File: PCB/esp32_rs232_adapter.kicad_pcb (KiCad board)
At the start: 2 copper layers, 46.5 x 57.7 mm, 46 parts, among them J1 Conn_01x04_Male, J2 DB9, J4 USB_B_Micro, Q1 IRF7404, SW2 Null_Modem_Selector, SW3 SW_SPST, U1 ESP32-WROOM-32D, U2 MAX3232, U3 TP4056, U4 AMS1117

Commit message: remove via in through hole
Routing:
- net Net-(J2-Pad3): vias 1 -> 0
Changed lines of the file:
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@@
     (thickness 1.6)
     (drawings 11)
-    (tracks 338)
+    (tracks 337)
     (zones 0)
     (modules 46)
@@
   (segment (start 161.671 123.885) (end 156.144001 129.411999) (width 0.25) (layer F.Cu) (net 32))
   (segment (start 153.38037 129.794) (end 152.249 129.794) (width 0.25) (layer F.Cu) (net 32))
-  (via (at 155.019 129.794) (size 0.8) (drill 0.4) (layers F.Cu B.Cu) (net 33))
   (segment (start 156.591 122.415) (end 156.591 128.222) (width 0.25) (layer F.Cu) (net 33))
   (segment (start 156.591 128.222) (end 155.019 129.794) (width 0.25) (layer F.Cu) (net 33))

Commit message: update
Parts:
- U2: footprint Package_SO:SSOP-16_5.3x6.2mm_P0.65mm -> Package_SO:SOP-16_4.55x10.3mm_P1.27mm
- moved U2 1.92 mm to (153.9, 115.8)
- renumbered Flash to SW1
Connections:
- J2 pad 9: (no net) -> Net-(J2-Pad9)
- J4 pad 2: (no net) -> Net-(J4-Pad2)
- J4 pad 3: (no net) -> Net-(J4-Pad3)
- J4 pad 4: (no net) -> Net-(J4-Pad4)
- U1 pad 11: (no net) -> Net-(U1-Pad11)
- U1 pad 12: (no net) -> Net-(U1-Pad12)
- U1 pad 13: (no net) -> Net-(U1-Pad13)
- U1 pad 14: (no net) -> Net-(U1-Pad14)
- U1 pad 16: (no net) -> Net-(U1-Pad16)
- U1 pad 17: (no net) -> Net-(U1-Pad17)
- U1 pad 18: (no net) -> Net-(U1-Pad18)
- U1 pad 19: (no net) -> Net-(U1-Pad19)
- U1 pad 20: (no net) -> Net-(U1-Pad20)
- U1 pad 21: (no net) -> Net-(U1-Pad21)
- U1 pad 22: (no net) -> Net-(U1-Pad22)
- U1 pad 23: (no net) -> Net-(U1-Pad23)
- U1 pad 26: (no net) -> Net-(U1-Pad26)
- U1 pad 27: (no net) -> Net-(U1-Pad27)
- U1 pad 28: (no net) -> Net-(U1-Pad28)
- U1 pad 29: (no net) -> Net-(U1-Pad29)
- U1 pad 30: (no net) -> Net-(U1-Pad30)
- U1 pad 32: (no net) -> Net-(U1-Pad32)
- U1 pad 33: (no net) -> Net-(U1-Pad33)
- U1 pad 5: (no net) -> Net-(U1-Pad5)
- U1 pad 6: (no net) -> Net-(U1-Pad6)
- U1 pad 7: (no net) -> Net-(U1-Pad7)
- U1 pad 8: (no net) -> Net-(U1-Pad8)
- U1 pad 9: (no net) -> Net-(U1-Pad9)
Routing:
- net /CTS: track 22.9 -> 0.00 mm, vias 1 -> 0
- net /TXD_RS232: track 22.4 -> 0.00 mm, vias 1 -> 0
- net /RXD_RS232: track 20.1 -> 0.00 mm, vias 1 -> 0
- net /CTS_RS232: track 17.3 -> 0.00 mm, vias 1 -> 0
- net /TXD: track 37.1 -> 22.9 mm
- net /RTS_RS232: track 13.8 -> 0.00 mm, vias 3 -> 0
- net /RXD: track 35.7 -> 23.9 mm
- net Net-(C2-Pad2): track 4.86 -> 0.00 mm
- net +3V3: track 35.6 -> 30.7 mm
- net GND: track 17.9 -> 13.1 mm, vias 8 -> 7
- net Net-(C5-Pad1): track 4.16 -> 0.00 mm
- net Net-(C6-Pad2): track 3.79 -> 0.00 mm
- net Net-(C4-Pad2): track 3.09 -> 0.00 mm
- net Net-(C4-Pad1): track 2.71 -> 0.00 mm
- net Net-(C2-Pad1): track 2.56 -> 0.00 mm
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
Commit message: work in progress with stuff for cb testing
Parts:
- removed D1: GREEN_LED, LED_SMD:LED_0805_2012Metric
- removed D2: RED_LED, LED_SMD:LED_0805_2012Metric
- added C12: 0.1uF, Capacitor_SMD:C_0805_2012Metric, F.Cu at (125.6, 99.7)
- added C13: 1nF, Capacitor_SMD:C_0805_2012Metric, F.Cu at (129.0, 99.7)
- added C14: 0.1uF, Capacitor_SMD:C_0805_2012Metric, F.Cu at (132.4, 99.7)
- added C15: 10nF, Capacitor_SMD:C_0805_2012Metric, F.Cu at (135.8, 99.7)
- added C16: 0.1nF, Capacitor_SMD:C_0805_2012Metric, F.Cu at (139.2, 99.7)
- added C17: 0.1uF, Capacitor_SMD:C_0805_2012Metric, F.Cu at (142.6, 99.7)
- added C18: 2.2nF, Capacitor_SMD:C_0805_2012Metric, F.Cu at (125.6, 101.6)
- added J3: Shunt-, Connector:Banana_Jack_1Pin, F.Cu at (107.3, 133.1)
- added J5: Common, Connector:Banana_Jack_1Pin, F.Cu at (107.5, 58.1)
- added J6: Shunt+, Connector:Banana_Jack_1Pin, F.Cu at (107.3, 118.1)
- added R15: 3k3, Resistor_SMD:R_0805_2012Metric, F.Cu at (129.0, 101.6)
- added R16: 10k, Resistor_SMD:R_0805_2012Metric, F.Cu at (132.4, 101.6)
- added R17: 10k, Resistor_SMD:R_0805_2012Metric, F.Cu at (135.8, 101.6)
- added R18: 10k, Resistor_SMD:R_0805_2012Metric, F.Cu at (139.2, 101.6)
- added U5: ACS712xLCTR-30A, Package_SO:SOIC-8_3.9x4.9mm_P1.27mm, F.Cu at (116.9, 124.9)
- added U6: MPU-6050, Sensor_Motion:InvenSense_QFN-24_4x4mm_P0.5mm, F.Cu at (121.2, 101.4)
- C10: value 10n -> 1u
- C11: value 1u -> 10n
- J1: value Conn_01x04_Male -> USB_B_Micro; footprint Connector_PinHeader_2.54mm:PinHeader_1x04_P2.54mm_Vertical -> power_supplies:USB_Micro-B_Molex-105017-0001
- J4: value USB_B_Micro -> Poles; footprint power_supplies:USB_Micro-B_Molex-105017-0001 -> Connector:Banana_Jack_3Pin
- U1: footprint RF_Module:ESP32-WROOM-32 -> power_supplies:ESP32-WROOM-32-Heat
- moved J1 109.8 mm to (260.5, 99.8)
- moved BT1 86.8 mm to (259.2, 121.6)
- moved R6 85.2 mm to (256.2, 118.0)
- moved R7 85.2 mm to (260.0, 114.1)
- moved R8 85.2 mm to (262.1, 114.1)
- moved C7 85.2 mm to (254.0, 118.0)
- moved F1 85.2 mm to (256.6, 106.8)
- moved U3 85.2 mm to (255.8, 112.4)
- moved C8 85.0 mm to (251.9, 114.5)
- moved R10 85.0 mm to (251.9, 110.9)
- moved R11 85.0 mm to (251.9, 107.4)
- moved R9 85.0 mm to (251.9, 119.8)
- moved D4 85.0 mm to (252.0, 90.2)
- moved Q1 85.0 mm to (254.6, 114.9)
- moved R13 85.0 mm to (251.8, 87.1)
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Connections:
- J1 pad 1: /RXD -> /power_supply/P5_0
- J1 pad 2: /TXD -> (no net)
- J1 pad 3: +3V3 -> (no net)
- J1 pad 4: GND -> (no net)
- J2 pad 9: Net-(J2-Pad9) -> (no net)
- J4 pad 1: /power_supply/P5_0 -> /Aph
- J4 pad 2: Net-(J4-Pad2) -> /Bph
- J4 pad 3: Net-(J4-Pad3) -> /Cph
- R10 pad 1: /power_supply/P_Batt_1 -> +BATT
- R10 pad 2: /power_supply/Vbatt_sig -> Net-(Q1-Pad4)
- R11 pad 1: /power_supply/Vbatt_sig -> /power_supply/P_Batt_1
- R11 pad 2: GND -> /Vbatt_sig
- R14 pad 1: +BATT -> /Vbatt_sig
- R14 pad 2: Net-(Q1-Pad4) -> GND
- R7 pad 2: Net-(D1-Pad2) -> /ChargePwrStatus
- R8 pad 2: Net-(D2-Pad2) -> /ChargeStatus
- U1 pad 10: Net-(R12-Pad1) -> /Aph
- U1 pad 11: Net-(U1-Pad11) -> /Bph
- U1 pad 12: Net-(U1-Pad12) -> /Cph
- U1 pad 13: Net-(U1-Pad13) -> (no net)
- U1 pad 14: Net-(U1-Pad14) -> /I_sense
- U1 pad 16: Net-(U1-Pad16) -> (no net)
- U1 pad 17: Net-(U1-Pad17) -> (no net)
- U1 pad 18: Net-(U1-Pad18) -> (no net)
- U1 pad 19: Net-(U1-Pad19) -> (no net)
- U1 pad 20: Net-(U1-Pad20) -> (no net)
- U1 pad 21: Net-(U1-Pad21) -> (no net)
- U1 pad 22: Net-(U1-Pad22) -> (no net)
- U1 pad 23: Net-(U1-Pad23) -> (no net)
- U1 pad 26: Net-(U1-Pad26) -> (no net)
- U1 pad 27: Net-(U1-Pad27) -> (no net)
- U1 pad 28: Net-(U1-Pad28) -> /Vbatt_sig
- U1 pad 29: Net-(U1-Pad29) -> (no net)
- U1 pad 30: Net-(U1-Pad30) -> /ChargeStatus
- U1 pad 32: Net-(U1-Pad32) -> (no net)
- U1 pad 33: Net-(U1-Pad33) -> /ChargePwrStatus
- U1 pad 37: Net-(R13-Pad1) -> (no net)
- U1 pad 4: /power_supply/Vbatt_sig -> Net-(R13-Pad1)
- U1 pad 5: Net-(U1-Pad5) -> Net-(R12-Pad1)
- U1 pad 6: Net-(U1-Pad6) -> /mpu_SCL
- U1 pad 7: Net-(U1-Pad7) -> /mpu_INT
- U1 pad 8: Net-(U1-Pad8) -> /mpu_SDA
- U1 pad 9: Net-(U1-Pad9) -> (no net)
- U3 pad 6: Net-(D1-Pad1) -> /ChargePwrStatus
- U3 pad 7: /power_supply/charge_status -> /ChargeStatus
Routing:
- net /power_supply/Vbatt_sig: track 56.8 -> 0.00 mm, vias 2 -> 0
- net /power_supply/P_Batt_1: track 50.4 -> 0.00 mm, vias 2 -> 0
- net Net-(R3-Pad2): track 33.3 -> 0.00 mm, vias 5 -> 0
- net /RTS: track 33.2 -> 0.00 mm, vias 1 -> 0
- net Net-(J2-Pad7): track 32.3 -> 0.00 mm, vias 2 -> 0
- net +3V3: track 30.7 -> 0.00 mm, vias 3 -> 0
- net /power_supply/P5_0: track 25.2 -> 0.00 mm, vias 2 -> 0
- net Net-(J2-Pad2): track 24.6 -> 0.00 mm, vias 1 -> 0
- net /RXD: track 23.9 -> 0.00 mm, vias 3 -> 0
- net /TXD: track 22.9 -> 0.00 mm, vias 1 -> 0
- net Net-(J2-Pad8): track 18.3 -> 0.00 mm, vias 2 -> 0
- net +BATT: track 17.8 -> 0.00 mm, vias 1 -> 0
- net /power_supply/P5_1: track 16.2 -> 0.00 mm
- net Net-(J2-Pad3): track 15.6 -> 0.00 mm
- net Net-(Q1-Pad4): track 14.6 -> 0.00 mm
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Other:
- board size 46.5 x 57.7 mm -> 100 x 100 mm
- net class SuperPower added: clearance 0.3, trace_width 2.2, via_dia 2.5, via_drill 1

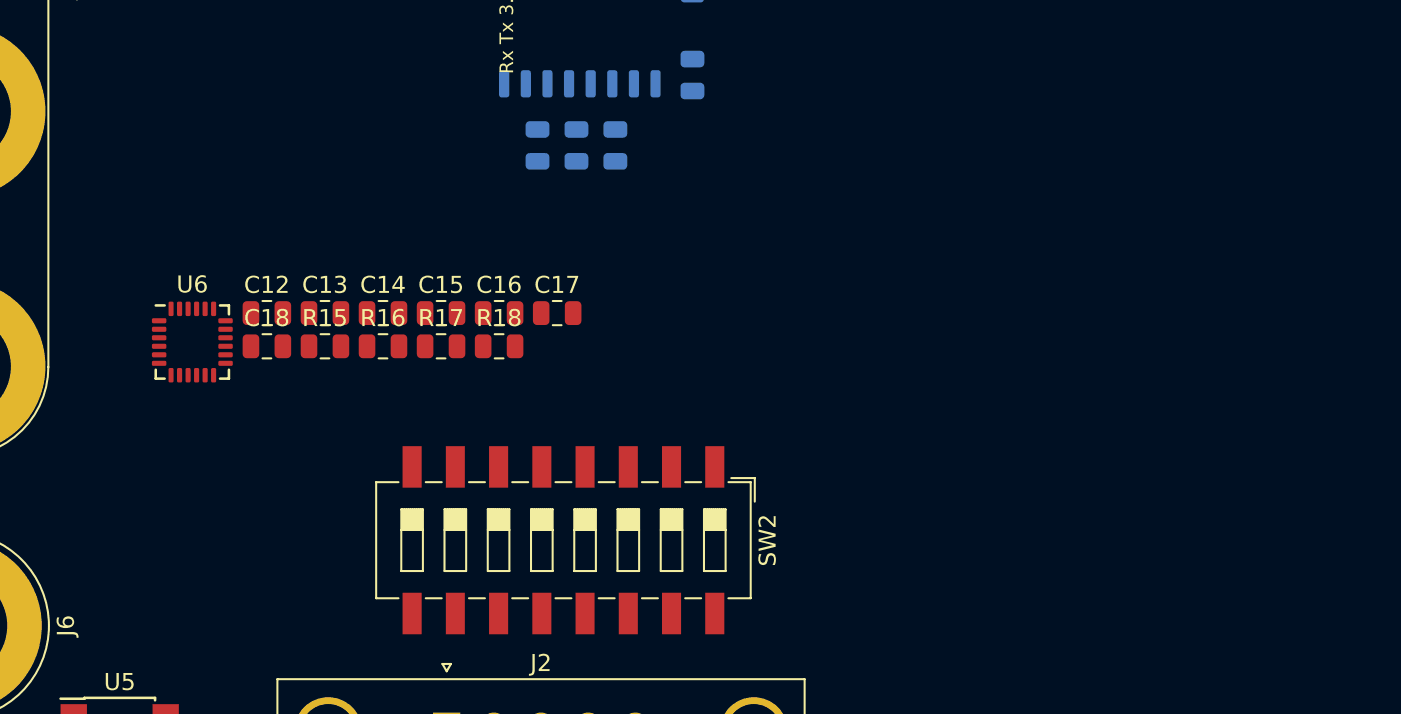
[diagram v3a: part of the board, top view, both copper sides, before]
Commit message: Updated pin assignments
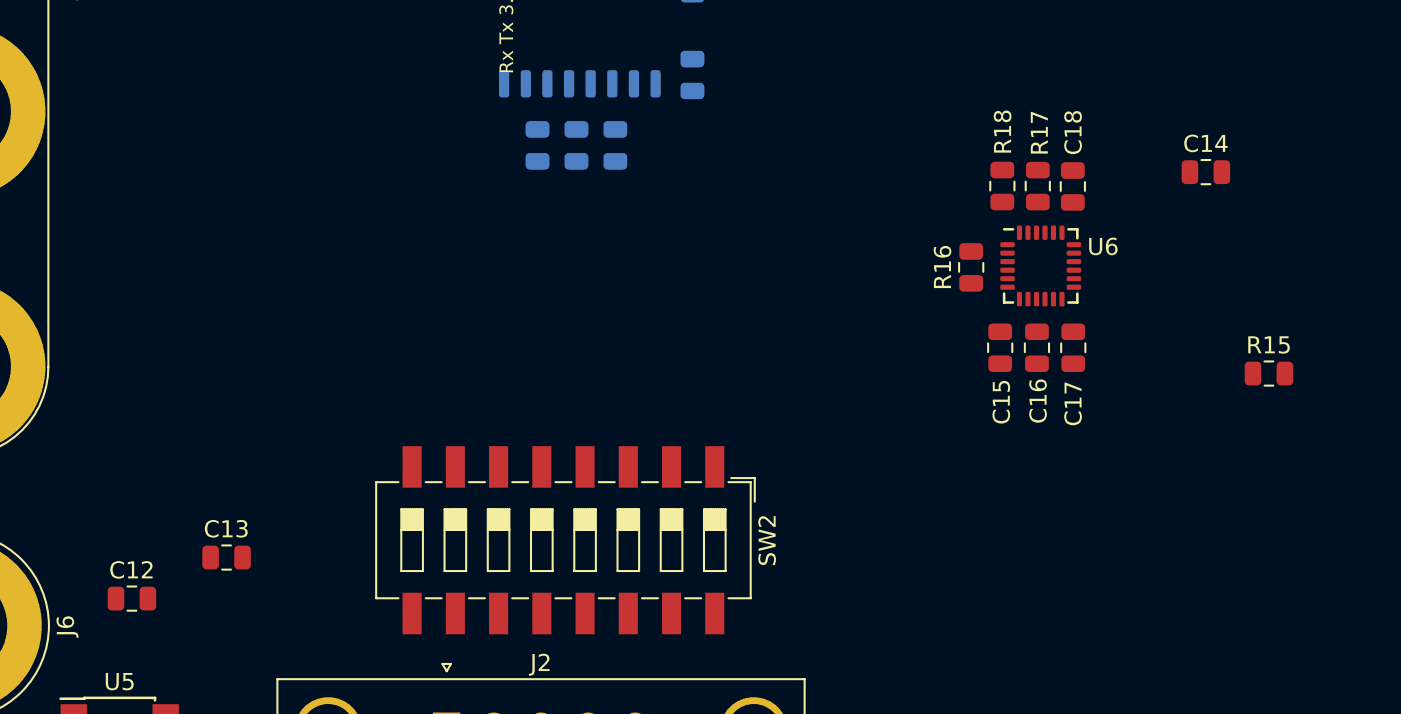
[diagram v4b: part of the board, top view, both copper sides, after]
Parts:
- moved R15 55.5 mm to (184.4, 103.2)
- moved U6 50.0 mm to (171.0, 96.9)
- moved C14 49.0 mm to (180.7, 91.4)
- moved C18 48.3 mm to (172.9, 92.3), turned to 90 degrees
- moved R17 36.3 mm to (170.9, 92.2), turned to 270 degrees
- moved R16 34.9 mm to (167.0, 97.0), turned to 90 degrees
- moved C15 32.9 mm to (168.7, 101.7), turned to 270 degrees
- moved C16 31.7 mm to (170.8, 101.7), turned to 270 degrees
- moved R18 31.0 mm to (168.8, 92.2), turned to 270 degrees
- moved C17 30.4 mm to (172.9, 101.7), turned to 270 degrees
- moved C12 18.5 mm to (117.7, 116.5)
- moved C13 15.5 mm to (123.2, 114.0)

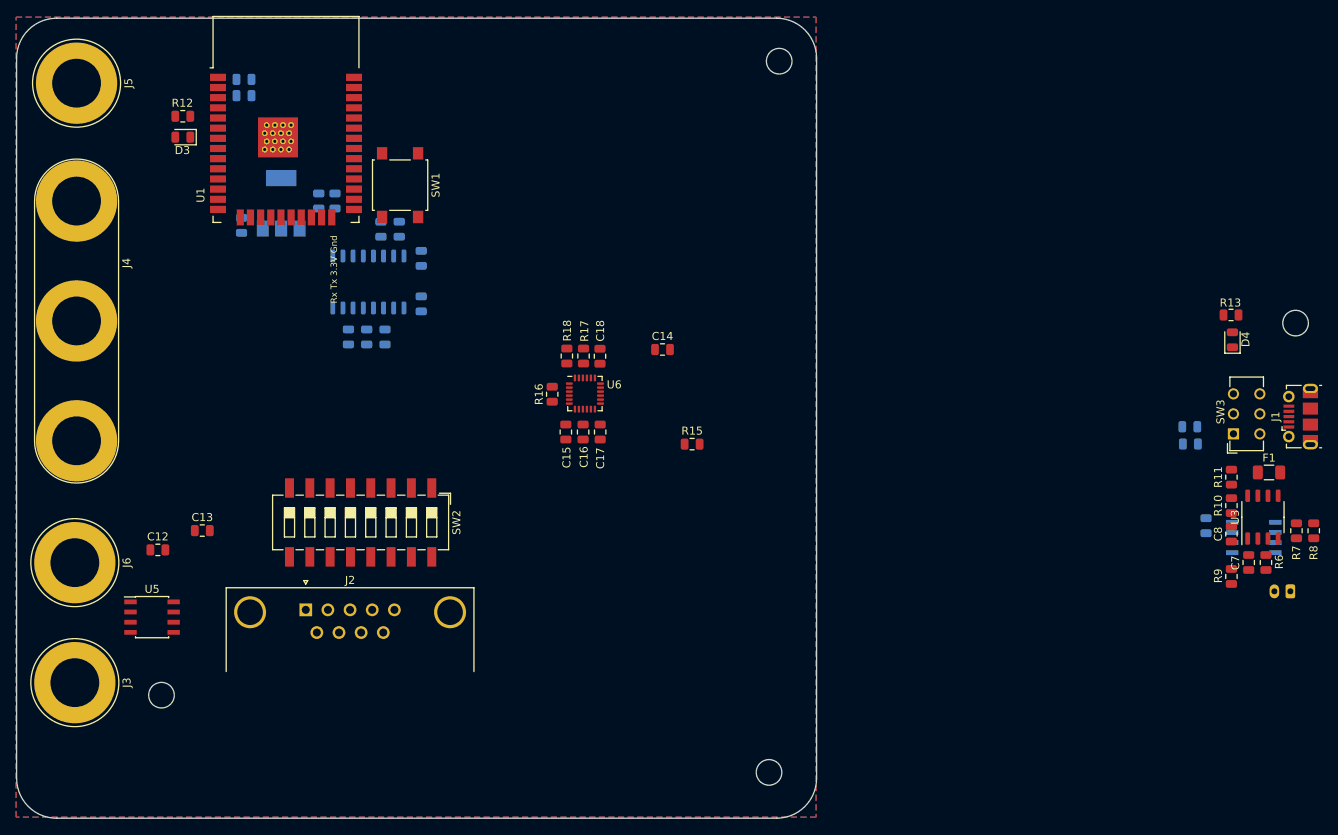
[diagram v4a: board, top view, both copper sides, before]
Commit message: remove null modem switch
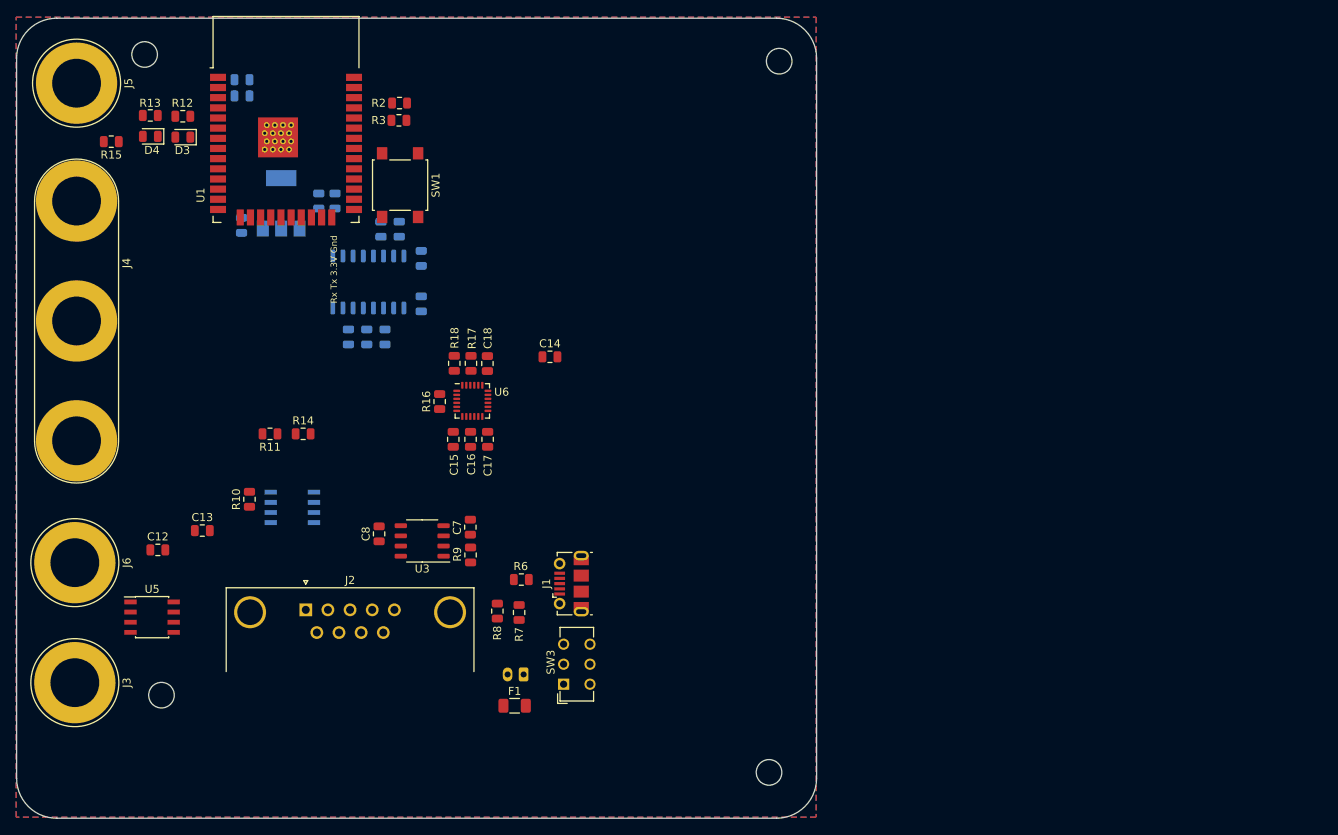
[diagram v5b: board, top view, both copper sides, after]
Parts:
- removed SW2: Null_Modem_Selector, Button_Switch_SMD:SW_DIP_SPSTx08_Slide_6.7x21.88mm_W8.61mm_P2.54mm_LowProfile
- R14, R2, R3: moved to F.Cu
- moved H1 147.7 mm to (116.0, 54.5)
- moved D4 137.6 mm to (116.7, 64.8), turned to 180 degrees
- moved R13 137.4 mm to (116.7, 62.2), turned to 180 degrees
- moved R10 122.7 mm to (129.1, 110.1)
- moved R11 120.3 mm to (131.7, 102.0), turned to 180 degrees
- moved Q1 120.2 mm to (134.5, 111.2)
- moved R14 113.4 mm to (135.8, 102.0), turned to 0 degrees
- moved R2 107.7 mm to (147.9, 60.6)
- moved C8 106.5 mm to (145.3, 114.5)
- moved R3 106.0 mm to (147.8, 62.8)
- moved U3 105.1 mm to (150.7, 115.3), turned to 180 degrees
- moved R8 102.5 mm to (160.1, 124.1)
- moved F1 98.7 mm to (162.3, 135.9)
- moved R7 97.7 mm to (162.8, 124.3)
- moved C7 97.4 mm to (156.7, 113.6)
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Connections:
- J2 pad 2: Net-(J2-Pad2) -> /TXD_RS232
- J2 pad 3: Net-(J2-Pad3) -> /RXD_RS232
- J2 pad 7: Net-(J2-Pad7) -> /CTS_RS232
- J2 pad 8: Net-(J2-Pad8) -> /RTS_RS232
